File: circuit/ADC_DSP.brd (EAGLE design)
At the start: 61 x 76.8 mm, 77 parts, among them IC1 REG1117, IC3 STM32F40XRXT6, IC4 CS4272, Q1 8MHz, Q2 24.576MHz

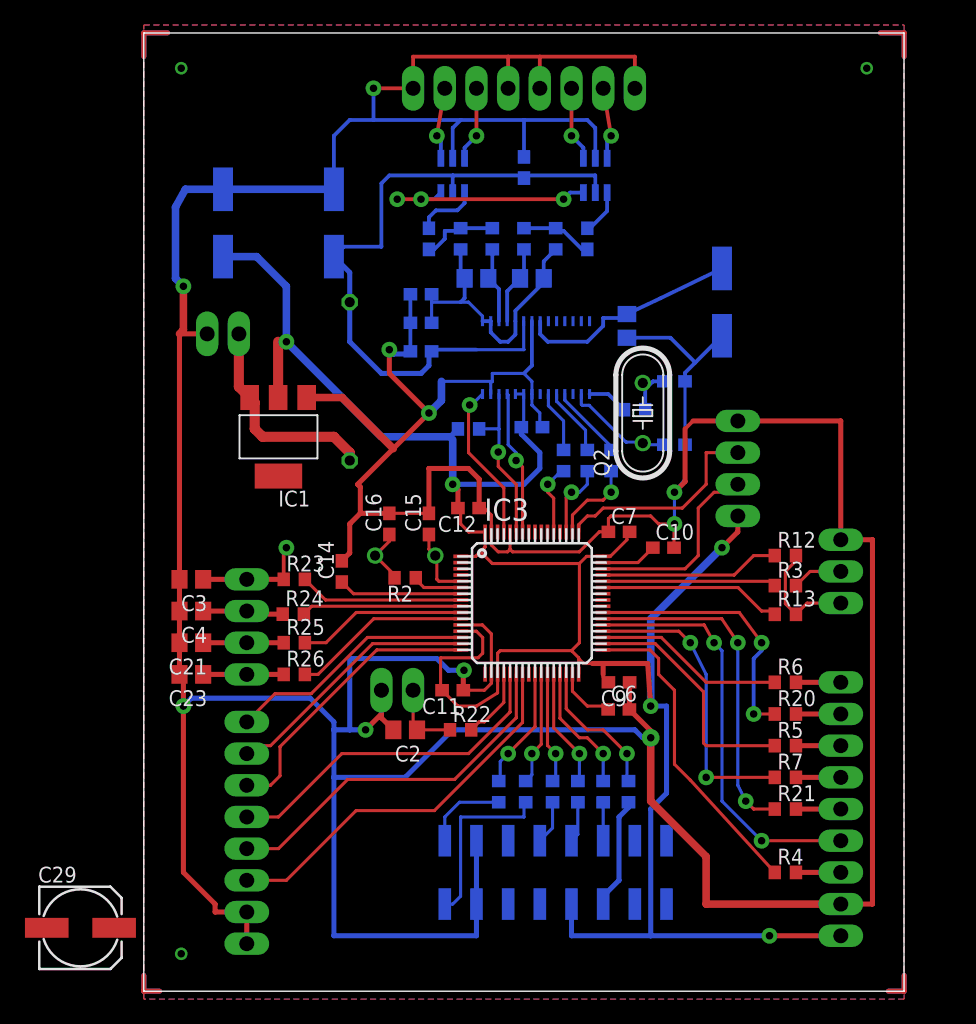
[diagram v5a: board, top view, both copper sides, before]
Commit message: - работающий в первом приближении USB Virtual Com Port
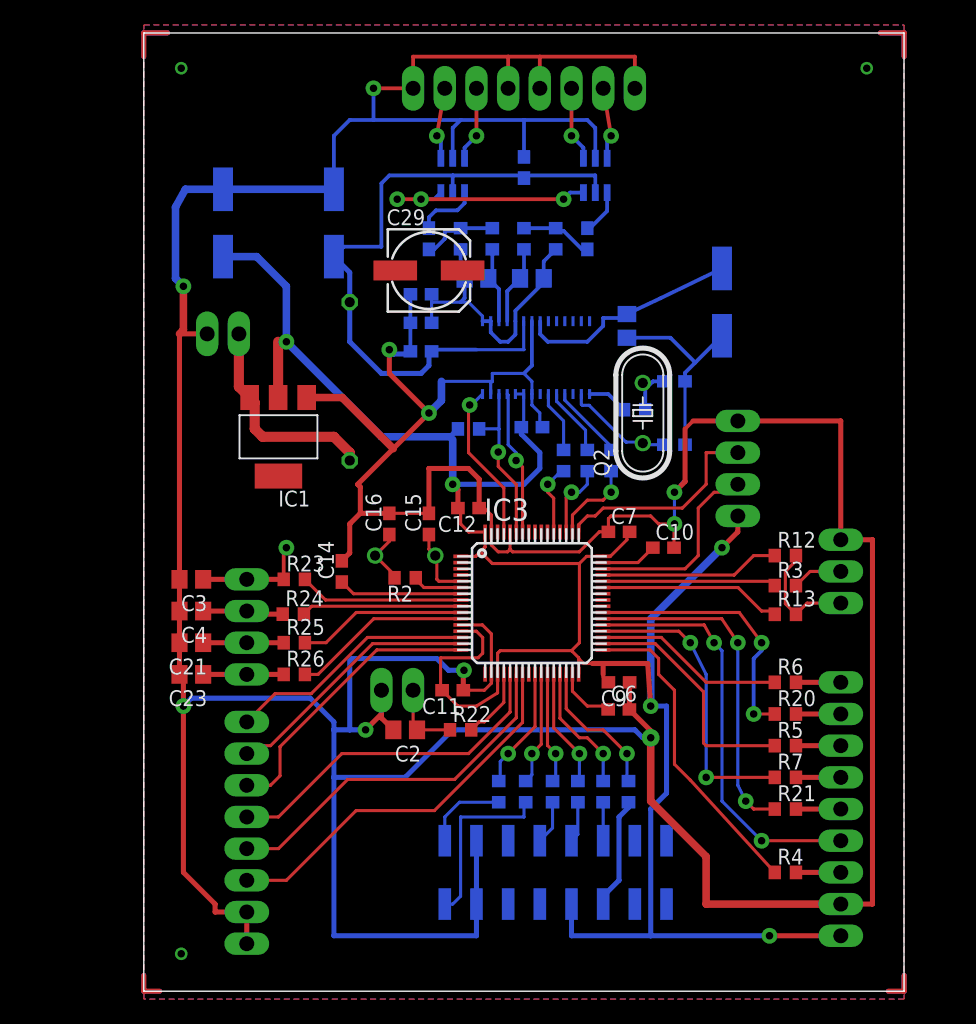
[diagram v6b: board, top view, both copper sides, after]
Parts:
- R13: value 1K5 -> 1K5(infinity)
- moved C29 59.7 mm to (22.9, 57.8)
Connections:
- net N$16 renamed D+
- net N$3 renamed D-
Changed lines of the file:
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@@
 <element name="R3" library="rcl" package="R0603" value="56" x="51.435" y="32.52"/>
 <element name="R12" library="rcl" package="R0603" value="56" x="51.435" y="34.925"/>
-<element name="R13" library="rcl" package="R0603" value="1K5" x="51.435" y="30.22"/>
+<element name="R13" library="rcl" package="R0603" value="1K5(infinity)" x="51.435" y="30.22"/>
 <element name="R14" library="rcl" package="R0603" value="33" x="32.77" y="16" rot="MR270"/>
 <element name="R15" library="rcl" package="R0603" value="33" x="34.8" y="16" rot="MR270"/>
@@
 </element>
 <element name="C13" library="rcl" package="C0603" value="100n" x="30.48" y="66.04" rot="MR90"/>
-<element name="C29" library="rcl" package="153CLV-0605" value="100uF" x="-5.08" y="5.08"/>
+<element name="C29" library="rcl" package="153CLV-0605" value="100uF" x="22.86" y="57.785"/>
 </elements>
 <signals>
@@
 <wire x1="3" y1="3" x2="5.715" y2="6.35" width="0" layer="19" extent="1-1"/>
 <wire x1="3" y1="74" x2="3.335" y2="64.295" width="0" layer="19" extent="16-16"/>
-<wire x1="-7.78" y1="5.08" x2="3" y2="3" width="0" layer="19" extent="1-1"/>
+<wire x1="20.16" y1="57.785" x2="3" y2="3" width="0" layer="19" extent="1-1"/>
 </signal>
 <signal name="+3V3">
@@
 <wire x1="25.4" y1="57.47" x2="25.72" y2="57.15" width="0.3048" layer="16"/>
 <contactref element="C29" pad="+"/>
-<wire x1="-2.38" y1="5.08" x2="23.075" y2="53.59" width="0" layer="19" extent="1-16"/>
+<wire x1="25.56" y1="57.785" x2="23.075" y2="53.59" width="0" layer="19" extent="1-16"/>
 </signal>
 <signal name="AVCC">
@@
 <wire x1="48.895" y1="34.925" x2="50.585" y2="34.925" width="0.25" layer="1"/>
 </signal>
-<signal name="N$16">
+<signal name="D+">
 <contactref element="R12" pad="2"/>
 <contactref element="R13" pad="2"/>
@@
 <wire x1="14.57" y1="31.365" x2="12.915" y2="33.02" width="0.25" layer="1"/>
 </signal>
-<signal name="N$3">
+<signal name="D-">
 <contactref element="R3" pad="2"/>
 <contactref element="USB" pad="2"/>
